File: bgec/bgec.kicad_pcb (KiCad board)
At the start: 2 copper layers, 1 part

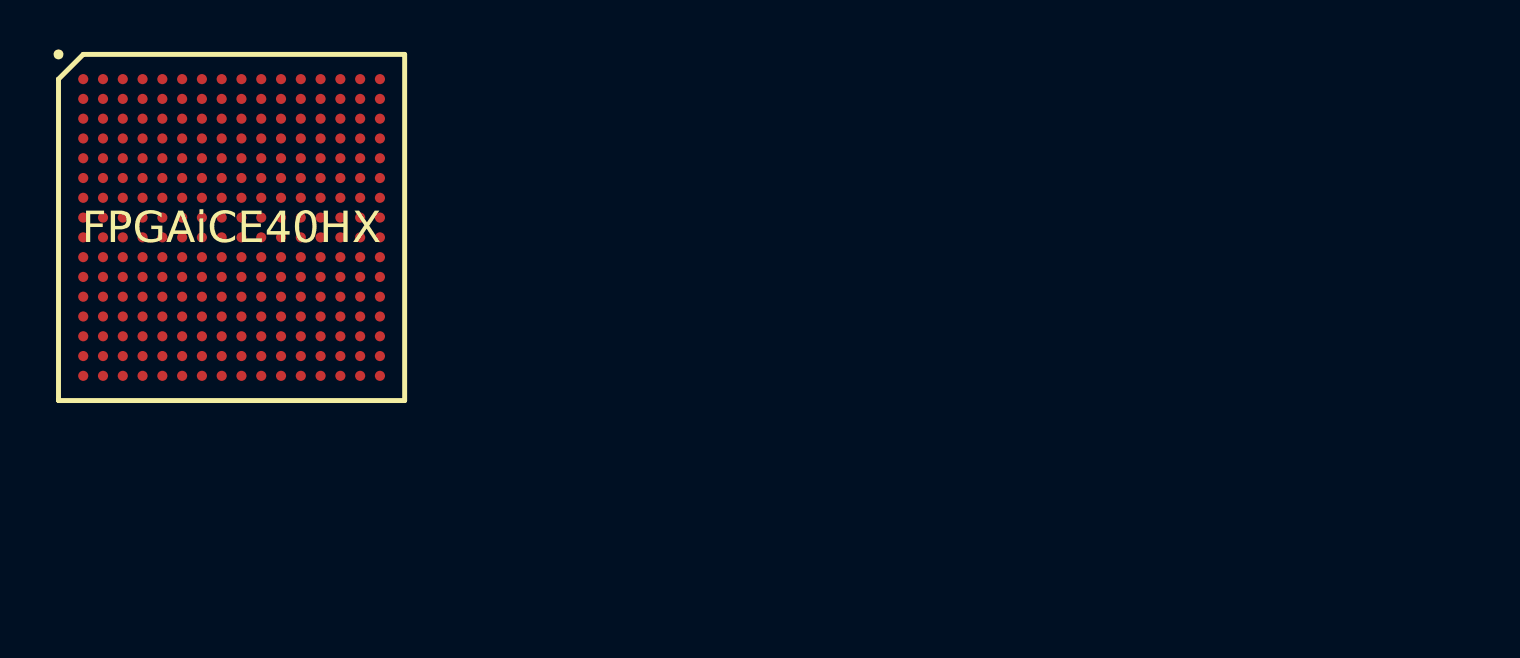
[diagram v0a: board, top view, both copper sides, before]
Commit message: Annotate items so PCB can be generated
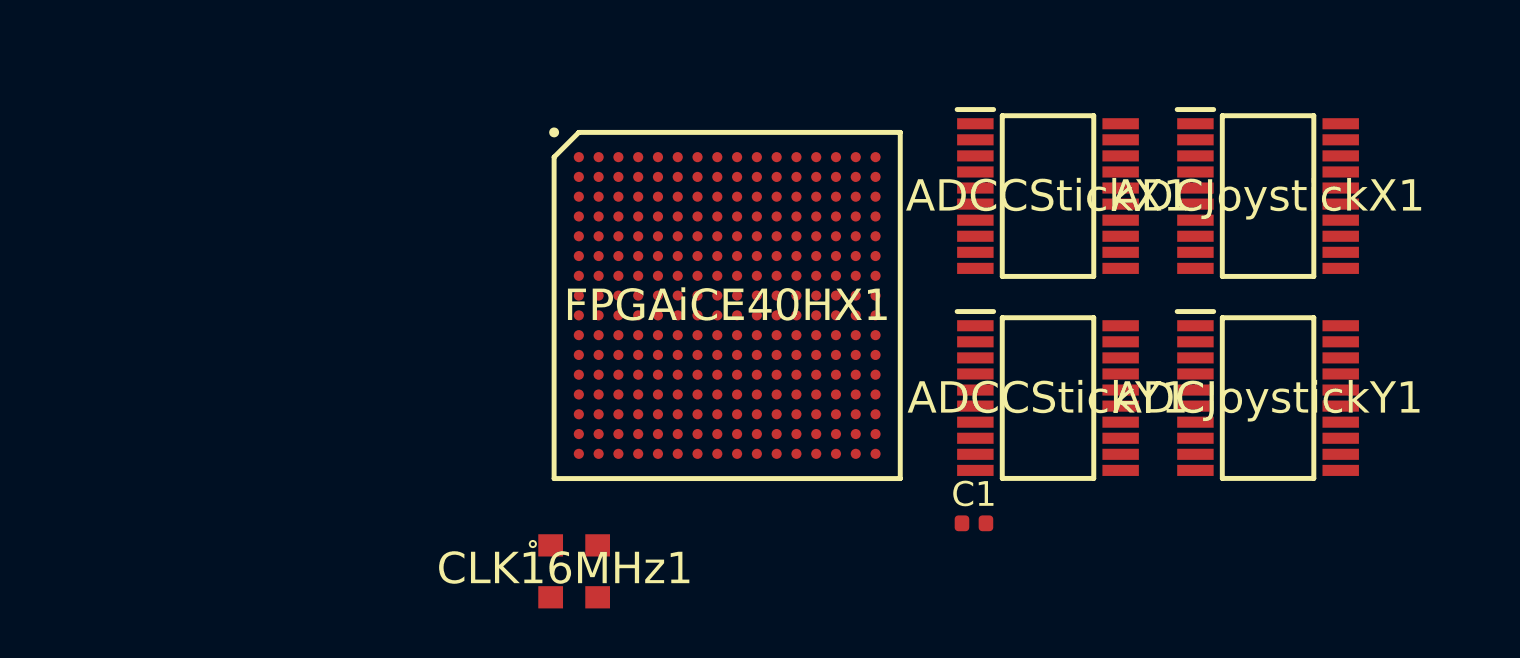
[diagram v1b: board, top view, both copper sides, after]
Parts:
- removed FPGAiCE40HX: BGA256C80P16X16_1400X1400X170, bgec:BGA256C80P16X16_1400X1400X170
- added ADCCStickX1: AD7822BRUZ, LibraryLoader:SOP65P640X120-20N, F.Cu at (153.7, 94.0)
- added ADCCStickY1: AD7822BRUZ, LibraryLoader:SOP65P640X120-20N, F.Cu at (153.7, 102.2)
- added ADCJoystickX1: AD7822BRUZ, LibraryLoader:SOP65P640X120-20N, F.Cu at (162.6, 94.0)
- added ADCJoystickY1: AD7822BRUZ, LibraryLoader:SOP65P640X120-20N, F.Cu at (162.6, 102.2)
- added C1: 100nF, Capacitor_SMD:C_0402_1005Metric, F.Cu at (150.7, 107.2)
- added CLK16MHz1: DSC6001CI2A-016.0000T, LibraryLoader:4-LEAD_CDFN-3.2X2.5_1, F.Cu at (134.5, 109.2)
- added FPGAiCE40HX1: ICE40HX8K-CT256, bgec:BGA256C80P16X16_1400X1400X170, F.Cu at (140.7, 98.4)

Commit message: Add clock and reset connections
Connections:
- net Net-(FPGAiCE40HX1-PadF7) renamed RESET
- FPGAiCE40HX1 pad C8: Net-(FPGAiCE40HX1-PadC8) -> CLK

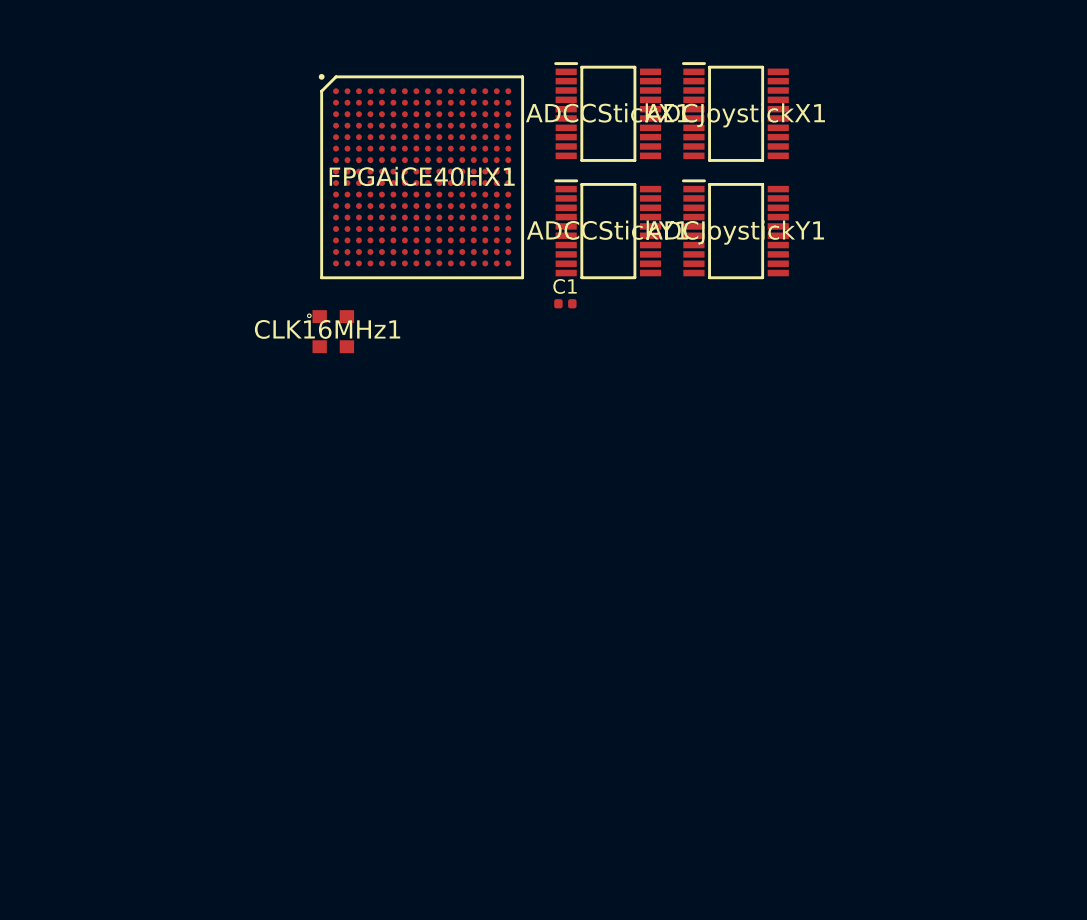
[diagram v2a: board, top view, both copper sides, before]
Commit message: Connect the ADCs
I might be doing this wrong by ignoring CONVST. We'll see. I need to update the software side of things to start doing Parallel ADCs.
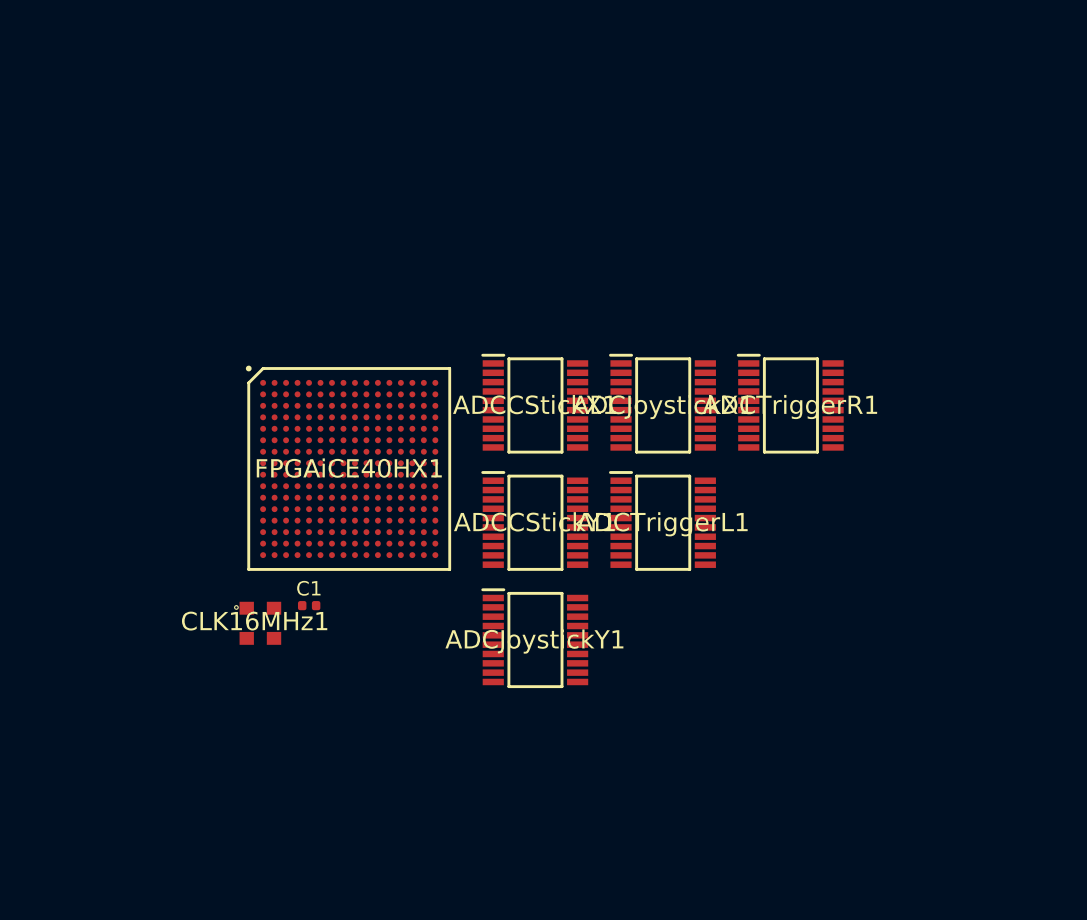
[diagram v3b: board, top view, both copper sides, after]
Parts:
- added ADCTriggerL1: AD7822BRUZ, LibraryLoader:SOP65P640X120-20N, F.Cu at (157.5, 122.5)
- added ADCTriggerR1: AD7822BRUZ, LibraryLoader:SOP65P640X120-20N, F.Cu at (166.4, 114.3)
- moved ADCJoystickY1 31.7 mm to (148.6, 130.6)
- moved C1 27.6 mm to (132.8, 128.2)
- moved CLK16MHz1 20.9 mm to (129.4, 129.5)
- moved ADCCStickX1 20.9 mm to (148.6, 114.3)
- moved ADCCStickY1 20.9 mm to (148.6, 122.5)
- moved ADCJoystickX1 20.9 mm to (157.5, 114.3)
- moved FPGAiCE40HX1 20.9 mm to (135.6, 118.7)
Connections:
- net Net-(ADCCStickX1-Pad8) renamed CStickXEOC
- net Net-(ADCCStickY1-Pad8) renamed CStickYEOC
- net Net-(FPGAiCE40HX1-PadA6) renamed ButtonL
- net Net-(FPGAiCE40HX1-PadA9) renamed ButtonZ
- net Net-(FPGAiCE40HX1-PadB3) renamed ModeMajor
- net Net-(FPGAiCE40HX1-PadC14) renamed GCData
- net Net-(FPGAiCE40HX1-PadC4) renamed ButtonR
- net Net-(FPGAiCE40HX1-PadC9) renamed ButtonB
- net Net-(FPGAiCE40HX1-PadD10) renamed ButtonA
- net Net-(FPGAiCE40HX1-PadD4) renamed ModeMinor
- net Net-(FPGAiCE40HX1-PadD9) renamed ButtonY
- net Net-(FPGAiCE40HX1-PadE9) renamed ButtonX
- net Net-(FPGAiCE40HX1-PadF9) renamed ButtonStart
- ADCCStickX1 pad 14: Net-(ADCCStickX1-Pad14) -> GCLogic
- ADCCStickX1 pad 7: Net-(ADCCStickX1-Pad7) -> GCLogicGround
- ADCCStickY1 pad 14: Net-(ADCCStickY1-Pad14) -> GCLogic
- ADCCStickY1 pad 7: Net-(ADCCStickY1-Pad7) -> GCLogicGround
- ADCJoystickX1 pad 1: Net-(ADCJoystickX1-Pad1) -> JoystickXDB2
- ADCJoystickX1 pad 14: Net-(ADCJoystickX1-Pad14) -> GCLogic
- ADCJoystickX1 pad 16: Net-(ADCJoystickX1-Pad16) -> JoystickXDB7
- ADCJoystickX1 pad 17: Net-(ADCJoystickX1-Pad17) -> JoystickXDB6
- ADCJoystickX1 pad 18: Net-(ADCJoystickX1-Pad18) -> JoystickXDB5
- ADCJoystickX1 pad 19: Net-(ADCJoystickX1-Pad19) -> JoystickXDB4
- ADCJoystickX1 pad 2: Net-(ADCJoystickX1-Pad2) -> JoystickXDB1
- ADCJoystickX1 pad 20: Net-(ADCJoystickX1-Pad20) -> JoystickXDB3
- ADCJoystickX1 pad 3: Net-(ADCJoystickX1-Pad3) -> JoystickXDB0
- ADCJoystickX1 pad 7: Net-(ADCJoystickX1-Pad7) -> GCLogicGround
- ADCJoystickX1 pad 8: Net-(ADCJoystickX1-Pad8) -> JoystickXEOC
- ADCJoystickY1 pad 1: Net-(ADCJoystickY1-Pad1) -> JoystickYDB2
- ADCJoystickY1 pad 14: Net-(ADCJoystickY1-Pad14) -> GCLogic
- ADCJoystickY1 pad 16: Net-(ADCJoystickY1-Pad16) -> JoystickYDB7
- ADCJoystickY1 pad 17: Net-(ADCJoystickY1-Pad17) -> JoystickYDB6
- ADCJoystickY1 pad 18: Net-(ADCJoystickY1-Pad18) -> JoystickYDB5
- ADCJoystickY1 pad 19: Net-(ADCJoystickY1-Pad19) -> JoystickYDB4
- ADCJoystickY1 pad 2: Net-(ADCJoystickY1-Pad2) -> JoystickYDB1
- ADCJoystickY1 pad 20: Net-(ADCJoystickY1-Pad20) -> JoystickYDB3
- ADCJoystickY1 pad 3: Net-(ADCJoystickY1-Pad3) -> JoystickYDB0
- ADCJoystickY1 pad 7: Net-(ADCJoystickY1-Pad7) -> GCLogicGround
- ADCJoystickY1 pad 8: Net-(ADCJoystickY1-Pad8) -> JoystickYEOC
- FPGAiCE40HX1 pad A1: Net-(FPGAiCE40HX1-PadA1) -> TriggerRDB1
- FPGAiCE40HX1 pad A10: Net-(FPGAiCE40HX1-PadA10) -> JoystickYDB1
- FPGAiCE40HX1 pad A11: Net-(FPGAiCE40HX1-PadA11) -> JoystickYDB0
- FPGAiCE40HX1 pad A15: Net-(FPGAiCE40HX1-PadA15) -> JoystickXDB1
- FPGAiCE40HX1 pad A16: Net-(FPGAiCE40HX1-PadA16) -> JoystickXDB2
- FPGAiCE40HX1 pad A2: Net-(FPGAiCE40HX1-PadA2) -> TriggerRDB3
- FPGAiCE40HX1 pad A5: Net-(FPGAiCE40HX1-PadA5) -> TriggerRDB7
- FPGAiCE40HX1 pad A7: Net-(FPGAiCE40HX1-PadA7) -> TriggerLDB5
- FPGAiCE40HX1 pad B10: Net-(FPGAiCE40HX1-PadB10) -> JoystickYDB4
- FPGAiCE40HX1 pad B11: Net-(FPGAiCE40HX1-PadB11) -> JoystickYDB3
- FPGAiCE40HX1 pad B12: Net-(FPGAiCE40HX1-PadB12) -> JoystickYDB5
- FPGAiCE40HX1 pad B13: Net-(FPGAiCE40HX1-PadB13) -> JoystickXDB0
- FPGAiCE40HX1 pad B14: Net-(FPGAiCE40HX1-PadB14) -> JoystickXDB6
- FPGAiCE40HX1 pad B15: Net-(FPGAiCE40HX1-PadB15) -> JoystickXEOC
- FPGAiCE40HX1 pad B4: Net-(FPGAiCE40HX1-PadB4) -> TriggerRDB4
- FPGAiCE40HX1 pad B5: Net-(FPGAiCE40HX1-PadB5) -> TriggerRDB6
- FPGAiCE40HX1 pad B6: Net-(FPGAiCE40HX1-PadB6) -> TriggerLDB2
- FPGAiCE40HX1 pad B7: Net-(FPGAiCE40HX1-PadB7) -> TriggerLDB3
- FPGAiCE40HX1 pad B8: Net-(FPGAiCE40HX1-PadB8) -> TriggerLDB6
- FPGAiCE40HX1 pad B9: Net-(FPGAiCE40HX1-PadB9) -> TriggerLEOC
- FPGAiCE40HX1 pad C10: Net-(FPGAiCE40HX1-PadC10) -> JoystickYDB2
- FPGAiCE40HX1 pad C11: Net-(FPGAiCE40HX1-PadC11) -> JoystickYDB7
- FPGAiCE40HX1 pad C12: Net-(FPGAiCE40HX1-PadC12) -> JoystickXDB5
- FPGAiCE40HX1 pad C13: Net-(FPGAiCE40HX1-PadC13) -> JoystickXDB3
- FPGAiCE40HX1 pad C5: Net-(FPGAiCE40HX1-PadC5) -> TriggerRDB0
- FPGAiCE40HX1 pad C6: Net-(FPGAiCE40HX1-PadC6) -> TriggerLDB1
- FPGAiCE40HX1 pad C7: Net-(FPGAiCE40HX1-PadC7) -> TriggerLDB4
- FPGAiCE40HX1 pad D11: Net-(FPGAiCE40HX1-PadD11) -> JoystickYDB6
- FPGAiCE40HX1 pad D13: Net-(FPGAiCE40HX1-PadD13) -> JoystickXDB7
- FPGAiCE40HX1 pad D5: Net-(FPGAiCE40HX1-PadD5) -> TriggerRDB2
- FPGAiCE40HX1 pad D6: Net-(FPGAiCE40HX1-PadD6) -> TriggerREOC
- FPGAiCE40HX1 pad D7: Net-(FPGAiCE40HX1-PadD7) -> TriggerLDB0
- FPGAiCE40HX1 pad D8: Net-(FPGAiCE40HX1-PadD8) -> TriggerLDB7
- FPGAiCE40HX1 pad E10: Net-(FPGAiCE40HX1-PadE10) -> JoystickYEOC
- FPGAiCE40HX1 pad E11: Net-(FPGAiCE40HX1-PadE11) -> JoystickXDB4
- FPGAiCE40HX1 pad E6: Net-(FPGAiCE40HX1-PadE6) -> TriggerRDB5

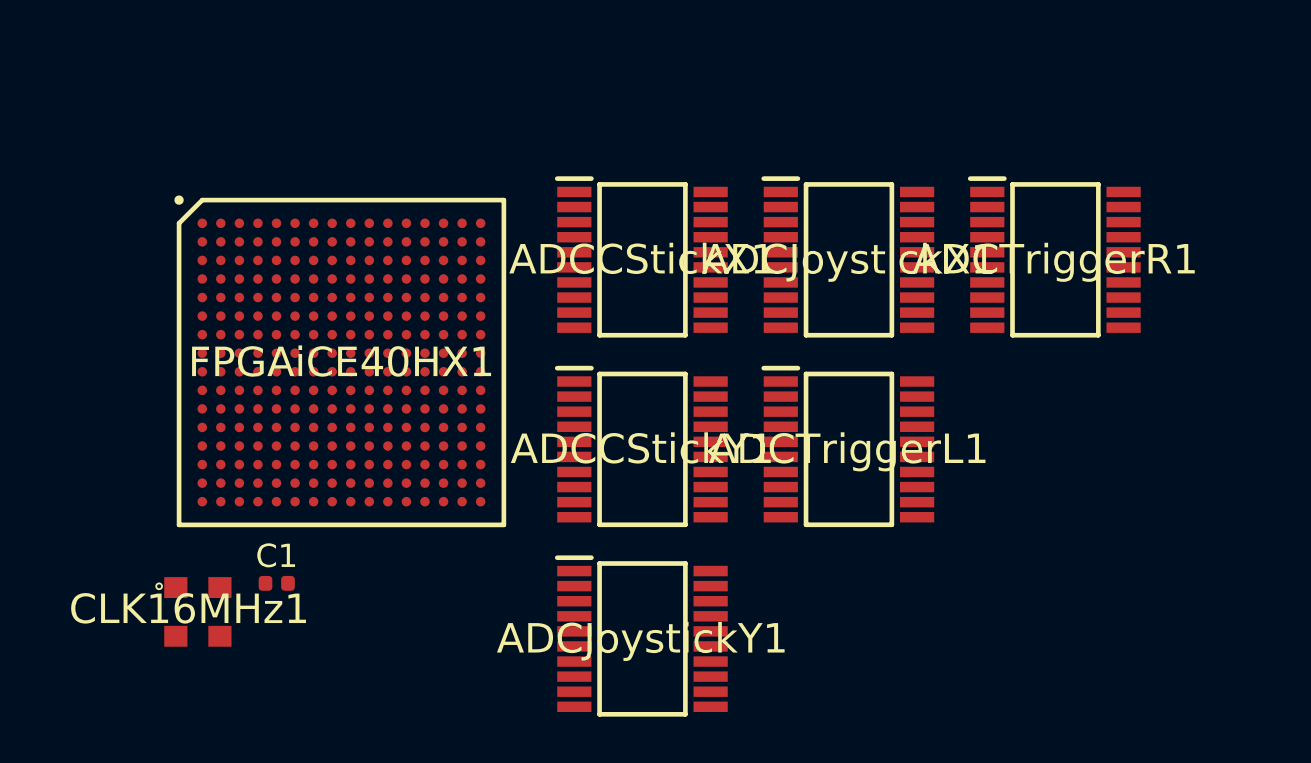
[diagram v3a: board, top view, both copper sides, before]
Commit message: Split into multiple sheets
Next problem to solve is routing. KiCad and Freerouter really hate that FPGA.
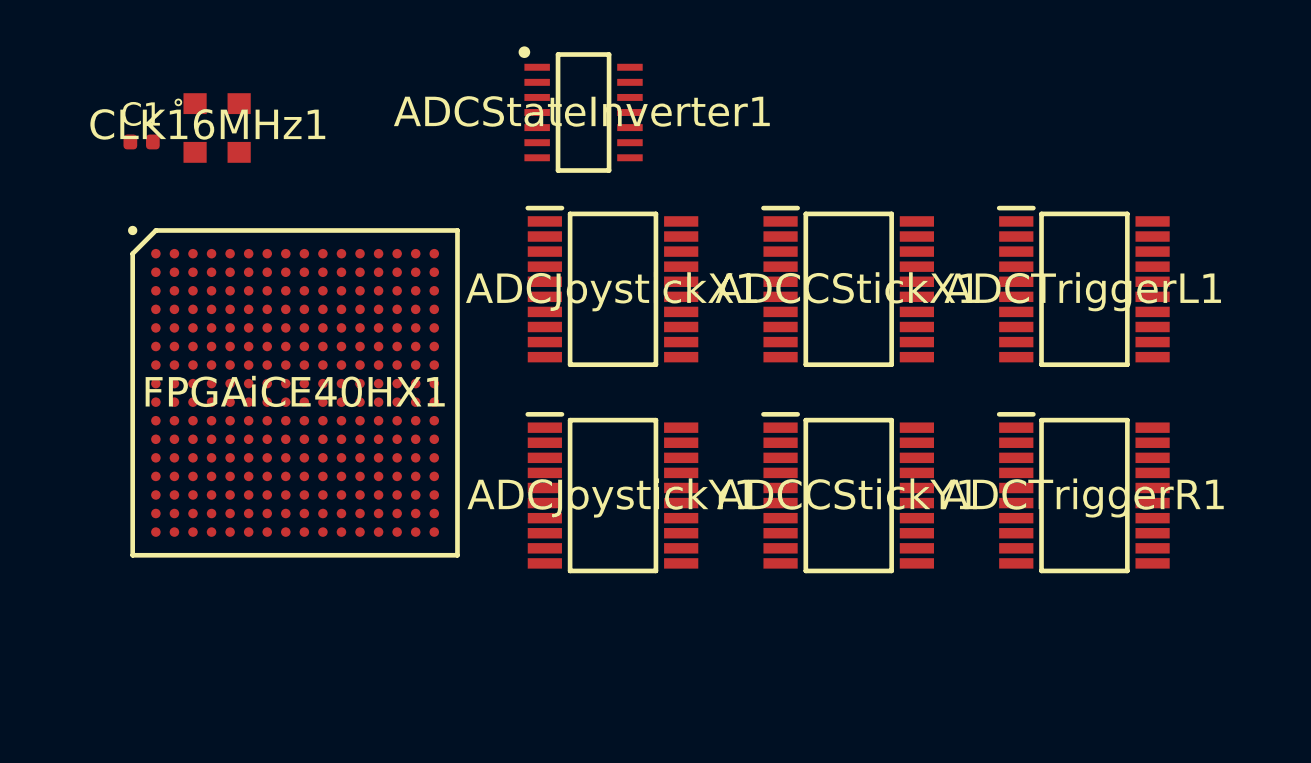
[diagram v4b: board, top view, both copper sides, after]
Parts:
- added ADCStateInverter1: 74HC04, LibraryLoader:SON65P440X500X110-14N, F.Cu at (146.1, 108.0)
- moved CLK16MHz1 20.9 mm to (130.3, 108.6)
- moved C1 19.9 mm to (127.0, 109.2)
- moved ADCTriggerL1 12.3 mm to (167.6, 115.6)
- moved ADCJoystickX1 10.2 mm to (147.3, 115.6)
- moved ADCTriggerR1 10.2 mm to (167.6, 124.5)
- moved ADCCStickY1 9.11 mm to (157.5, 124.5)
- moved ADCCStickX1 8.98 mm to (157.5, 115.6)
- moved ADCJoystickY1 6.31 mm to (147.3, 124.5)
- moved FPGAiCE40HX1 2.39 mm to (133.6, 120.0)
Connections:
- net ButtonStart renamed Net-(FPGAiCE40HX1-PadF9)
- net ButtonX renamed Net-(FPGAiCE40HX1-PadE9)
- net ButtonY renamed Net-(FPGAiCE40HX1-PadD9)
- net ButtonZ renamed Net-(FPGAiCE40HX1-PadA9)
- net ModeMajor renamed Net-(FPGAiCE40HX1-PadB3)
- net ModeMinor renamed Net-(FPGAiCE40HX1-PadD4)
- ADCCStickX1 pad 8: CStickXEOC -> CStickXNotEOC
- ADCCStickY1 pad 8: CStickYEOC -> CStickYNotEOC
- ADCJoystickX1 pad 8: JoystickXEOC -> JoystickXNotEOC
- ADCJoystickY1 pad 8: JoystickYEOC -> JoystickYNotEOC
- ADCTriggerL1 pad 8: TriggerLEOC -> TriggerLNotEOC
- ADCTriggerR1 pad 8: TriggerREOC -> TriggerRNotEOC
- FPGAiCE40HX1 pad A1: TriggerRDB1 -> TriggerRDB2
- FPGAiCE40HX1 pad A10: JoystickYDB1 -> JoystickYDB3
- FPGAiCE40HX1 pad A11: JoystickYDB0 -> JoystickYDB2
- FPGAiCE40HX1 pad A15: JoystickXDB1 -> JoystickXDB2
- FPGAiCE40HX1 pad A16: JoystickXDB2 -> JoystickXDB3
- FPGAiCE40HX1 pad A2: TriggerRDB3 -> TriggerRDB4
- FPGAiCE40HX1 pad A5: TriggerRDB7 -> TriggerREOC
- FPGAiCE40HX1 pad A6: ButtonL -> TriggerLDB0
- FPGAiCE40HX1 pad A7: TriggerLDB5 -> TriggerLDB6
- FPGAiCE40HX1 pad B10: JoystickYDB4 -> JoystickYDB6
- FPGAiCE40HX1 pad B11: JoystickYDB3 -> JoystickYDB5
- FPGAiCE40HX1 pad B12: JoystickYDB5 -> JoystickYDB7
- FPGAiCE40HX1 pad B13: JoystickXDB0 -> JoystickXDB1
- FPGAiCE40HX1 pad B14: JoystickXDB6 -> JoystickXDB7
- FPGAiCE40HX1 pad B15: JoystickXEOC -> Net-(FPGAiCE40HX1-PadB15)
- FPGAiCE40HX1 pad B4: TriggerRDB4 -> TriggerRDB5
- FPGAiCE40HX1 pad B5: TriggerRDB6 -> TriggerRDB7
- FPGAiCE40HX1 pad B6: TriggerLDB2 -> TriggerLDB3
- FPGAiCE40HX1 pad B7: TriggerLDB3 -> TriggerLDB4
- FPGAiCE40HX1 pad B8: TriggerLDB6 -> TriggerLDB7
- FPGAiCE40HX1 pad B9: TriggerLEOC -> Net-(FPGAiCE40HX1-PadB9)
- FPGAiCE40HX1 pad C10: JoystickYDB2 -> JoystickYDB4
- FPGAiCE40HX1 pad C11: JoystickYDB7 -> Net-(FPGAiCE40HX1-PadC11)
- FPGAiCE40HX1 pad C12: JoystickXDB5 -> JoystickXDB6
- FPGAiCE40HX1 pad C13: JoystickXDB3 -> JoystickXDB4
- FPGAiCE40HX1 pad C4: ButtonR -> TriggerRDB0
- FPGAiCE40HX1 pad C5: TriggerRDB0 -> TriggerRDB1
- FPGAiCE40HX1 pad C6: TriggerLDB1 -> TriggerLDB2
- FPGAiCE40HX1 pad C7: TriggerLDB4 -> TriggerLDB5
- FPGAiCE40HX1 pad C9: ButtonB -> JoystickYDB0
- FPGAiCE40HX1 pad D10: ButtonA -> JoystickYDB1
- FPGAiCE40HX1 pad D11: JoystickYDB6 -> JoystickYEOC
- FPGAiCE40HX1 pad D13: JoystickXDB7 -> JoystickXEOC
- FPGAiCE40HX1 pad D5: TriggerRDB2 -> TriggerRDB3
- FPGAiCE40HX1 pad D6: TriggerREOC -> Net-(FPGAiCE40HX1-PadD6)
- FPGAiCE40HX1 pad D7: TriggerLDB0 -> TriggerLDB1
- FPGAiCE40HX1 pad D8: TriggerLDB7 -> TriggerLEOC
- FPGAiCE40HX1 pad E10: JoystickYEOC -> JoystickXDB0
- FPGAiCE40HX1 pad E11: JoystickXDB4 -> JoystickXDB5
- FPGAiCE40HX1 pad E6: TriggerRDB5 -> TriggerRDB6
